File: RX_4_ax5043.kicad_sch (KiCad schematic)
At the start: 19 parts, among them P4 CONUFL001-SMD-T, Q6 DMP2160UWQ-7, U19 AX5043

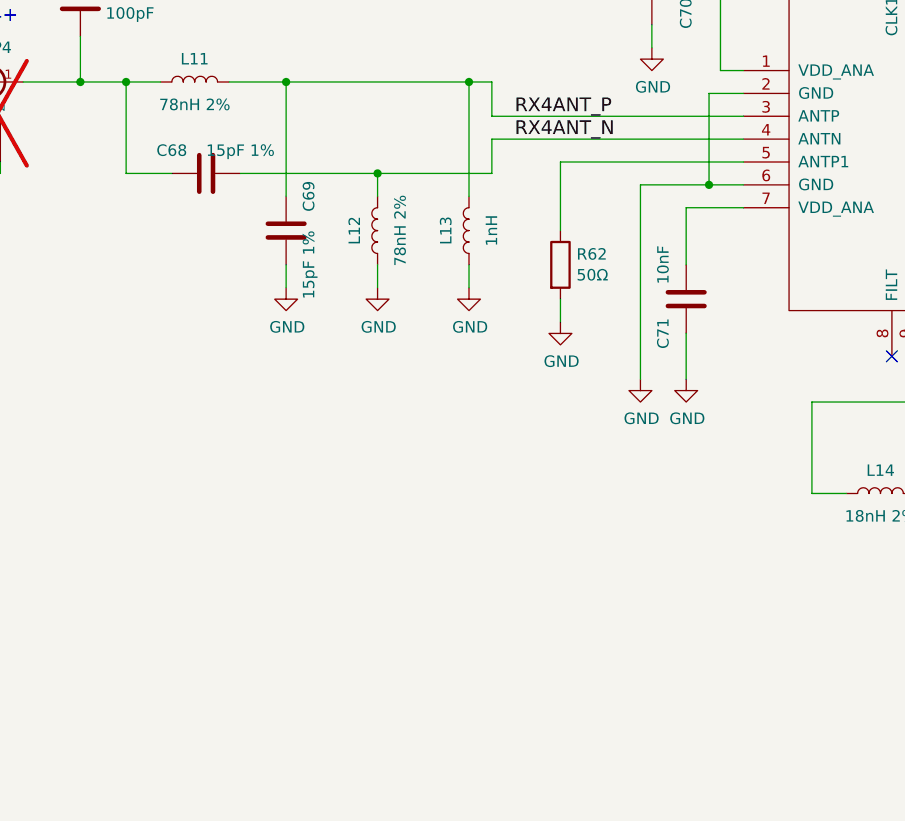
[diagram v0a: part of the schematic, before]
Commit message: Add a U.FL connector to ANTP1 on AX5043 RX4
Add it with a matching network, and add a matching network on the one on
the TX AX5043, too.  All DNP.

Signed-off-by: Corey Minyard <corey@minyard.net>
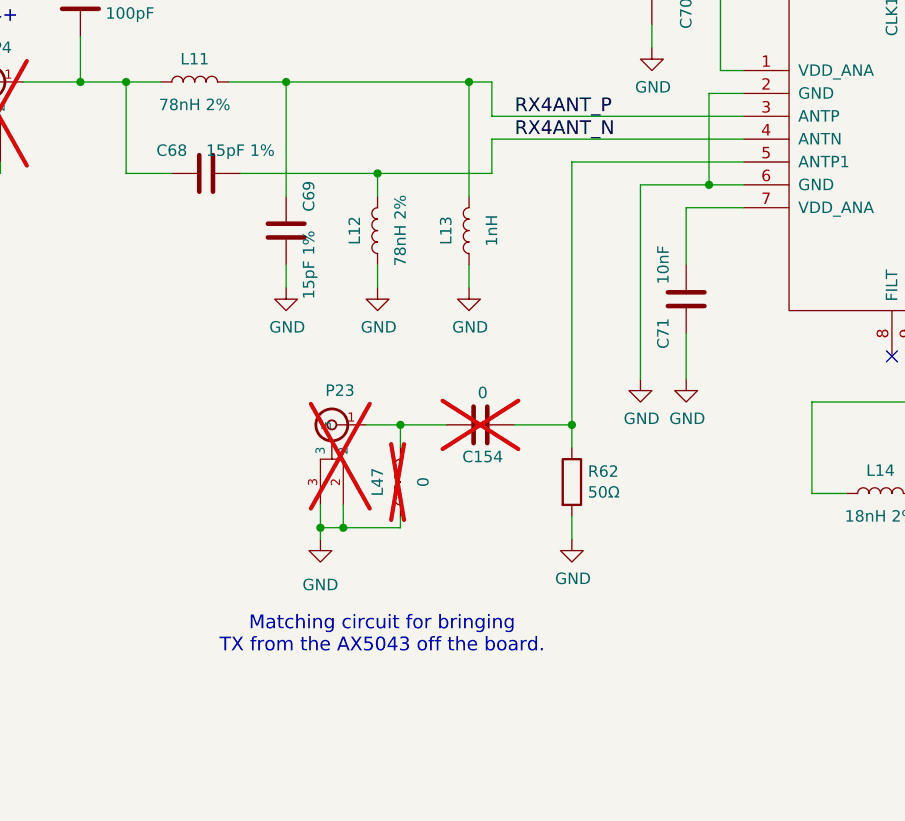
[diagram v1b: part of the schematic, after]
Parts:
- added C154: 0, Capacitor_SMD:C_0402_1005Metric_Pad0.74x0.62mm_HandSolder, symbol Device:C
- added L47: 0, Inductor_SMD:L_0402_1005Metric_Pad0.77x0.64mm_HandSolder, symbol Device:L
- added P23: CONUFL001-SMD-T, PacSatDev_misc:CONN1_CONUFL_TEC, symbol PACSAT_DEV_misc:U_FL
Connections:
- net GND: now also L47.1, P23.2, P23.3
- net at R62.1, U19.5 (ANTP1): now also C154.1
- new net: C154.2, L47.2, P23.1 (In)
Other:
- note added: "Matching circuit for bringing TX from the AX5043 off the board."
- moved on the sheet: R62

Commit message: Switch the 78nH parts on the RX AX5043 inputs to 75nH
78nH parts are not that available, especially in space ratings, so it
had to change.  I built a simulation and figured out what looks like a
reasonable approximation of the AX5043 (100 ohms differential?) and
changed the 78nH to 75nH and it didn't make a significant difference.

Signed-off-by: Corey Minyard <corey@minyard.net>
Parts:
- L11, L12: value 78nH 2% -> 75nH 2%
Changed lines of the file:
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@@
 			)
 		)
-		(property "Value" "78nH 2%"
+		(property "Value" "75nH 2%"
 			(at 154.94 142.24 90)
 			(effects
@@
 			)
 		)
-		(property "Value" "78nH 2%"
+		(property "Value" "75nH 2%"
 			(at 132.08 128.27 90)
 			(effects
